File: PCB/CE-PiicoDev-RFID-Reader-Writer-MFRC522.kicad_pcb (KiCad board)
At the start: 2 copper layers, 25.4 x 52 mm, 19 parts, among them J1 , J2 , J3 Conn_PiicoDev_header_01x04_Ma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

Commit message: Update all
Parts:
- added C1: 22p NP0, Capacitor_SMD:C_0402_1005Metric, F.Cu at (152.4, 99.5)
- added C10: NP0 2%, Capacitor_SMD:C_0603_1608Metric, F.Cu at (153.1, 92.1)
- added C11: 100n, Capacitor_SMD:C_0402_1005Metric, F.Cu at (155.3, 99.5)
- added C12: 100n, Capacitor_SMD:C_0402_1005Metric, F.Cu at (158.2, 95.5)
- added C13: 100n, Capacitor_SMD:C_0402_1005Metric, F.Cu at (155.3, 97.5)
- added C2: 1n NP0 10%, Capacitor_SMD:C_0603_1608Metric, F.Cu at (143.9, 97.3)
- added C3: 100n X7R 10%, Capacitor_SMD:C_0402_1005Metric, F.Cu at (146.6, 106.0)
- added C4: 22p NP0, Capacitor_SMD:C_0402_1005Metric, F.Cu at (158.2, 97.5)
- added C5: 120p NP0 2%, Capacitor_SMD:C_0603_1608Metric, F.Cu at (149.1, 92.8)
- added C6: 120p NP0 2%, Capacitor_SMD:C_0603_1608Metric, F.Cu at (160.7, 108.3)
- added C7: C, Capacitor_SMD:C_0603_1608Metric, F.Cu at (140.9, 99.8)
- added C8: C, Capacitor_SMD:C_0603_1608Metric, F.Cu at (147.9, 97.3)
- added C9: NP0 2%, Capacitor_SMD:C_0603_1608Metric, F.Cu at (144.9, 99.8)
- added D2: LED, CoreElectronics_Components:LED_1206_3216Metric_ReverseMount_Hole1.8x2.4mm, F.Cu at (97.3, 96.6)
- added J4: Conn_01x01_Male, Connector_PinHeader_1.27mm:PinHeader_1x01_P1.27mm_Vertical, F.Cu at (150.7, 89.2)
- added J5: Conn_01x01_Male, CoreElectronics_Components:PiicoDev_header_1pin_INT_uninverted, F.Cu at (103.4, 120.9)
- added JP3: SolderJumper_2_Bridged, CoreElectronics_Components:SolderJumper-2_P1.3mm_Bridged_RoundedPad1.0x1.5mm, B.Cu at (86.2, 101.3)
- added L1: 1uH, Inductor_SMD:L_0402_1005Metric, F.Cu at (156.6, 93.5)
- added L2: 1uH, Inductor_SMD:L_0402_1005Metric, F.Cu at (152.4, 97.6)
- added NT1: Net-Tie_2, PiicoDev RFID MFRC522:NetTie-2_SMD_Pad0.25mm, F.Cu at (97.3, 86.4)
- added NT2: Net-Tie_2, PiicoDev RFID MFRC522:NetTie-2_SMD_Pad0.25mm, F.Cu at (97.3, 85.9)
- added NT3: Net-Tie_2, PiicoDev RFID MFRC522:NetTie-2_SMD_Pad0.25mm, F.Cu at (97.3, 85.4)
- added NT4: Net-Tie_2, PiicoDev RFID MFRC522:NetTie-2_SMD_Pad0.25mm, B.Cu at (97.3, 85.9)
- added NT5: Net-Tie_2, PiicoDev RFID MFRC522:NetTie-2_SMD_Pad0.25mm, B.Cu at (97.3, 86.4)
- added R4: 820R, Resistor_SMD:R_0603_1608Metric, F.Cu at (158.8, 88.8)
- added R5: R, Resistor_SMD:R_0603_1608Metric, F.Cu at (151.9, 95.3)
- added R6: R, Resistor_SMD:R_0603_1608Metric, F.Cu at (96.5, 88.1)
- added R7: R, Resistor_SMD:R_0603_1608Metric, F.Cu at (98.1, 88.1)
- added R8: R, Resistor_SMD:R_0402_1005Metric, F.Cu at (155.3, 95.5)
- added U1: MFRC522, Package_DFN_QFN:VQFN-32-1EP_5x5mm_P0.5mm_EP3.1x3.1mm, F.Cu at (97.3, 101.3)
- added Y1: 27.12MHz 12pF, Crystal:Crystal_SMD_3225-4Pin_3.2x2.5mm, F.Cu at (102.8, 95.6)
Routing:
- net /TURN6: track 0.00 -> 95.3 mm, vias 0 -> 1
- net /TURN1: track 0.00 -> 93.7 mm
- net /TURN2: track 0.00 -> 91.1 mm
- net /TURN5: track 0.00 -> 90.7 mm
- net /TURN3: track 0.00 -> 88.0 mm
- net /TURN4: track 0.00 -> 87.8 mm, vias 0 -> 1
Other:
- board text added: "Designed at Core Electronics by Peter Johnston"
- board text removed: "Designed at Core Electronics"

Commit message: Update
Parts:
- added C14: 100n, Capacitor_SMD:C_0402_1005Metric, F.Cu at (102.5, 103.1)
- added R9: 4k7, Resistor_SMD:R_0402_1005Metric, F.Cu at (102.1, 100.6)
- FID1, FID2: footprint Fiducial:Fiducial_1mm_Mask2mm -> CoreElectronics_Components:Fiducial_1mm_Mask2mm_No_Courtyard
- Y1: footprint Crystal:Crystal_SMD_3225-4Pin_3.2x2.5mm -> Crystal:Crystal_SMD_TXC_7M-4Pin_3.2x2.5mm
- moved R4 65.9 mm to (93.7, 98.9), turned to 90 degrees
- moved C4 64.5 mm to (93.9, 102.3), turned to 180 degrees
- moved L1 62.9 mm to (93.7, 91.7), turned to 90 degrees
- moved C6 62.4 mm to (101.3, 89.2)
- moved C13 59.4 mm to (95.9, 98.2), turned to 90 degrees
- moved C1 59.4 mm to (93.0, 101.0)
- moved R5 59.2 mm to (92.7, 95.9), turned to 90 degrees
- moved C12 57.3 mm to (101.0, 98.7), turned to 180 degrees
- moved C11 56.1 mm to (99.2, 97.8), turned to 90 degrees
- moved C5 55.9 mm to (93.3, 89.2), turned to 270 degrees
- moved C10 54.2 mm to (98.9, 91.5)
- moved R8 54.0 mm to (101.4, 95.1), turned to 180 degrees
- moved C3 52.3 mm to (94.9, 98.2), turned to 270 degrees
- moved L2 51.8 mm to (100.9, 91.7), turned to 90 degrees
- moved C2 51.8 mm to (92.1, 98.9), turned to 270 degrees
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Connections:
- C11 pad 1: Net-(C11-Pad1) -> +3V3
- C12 pad 1: Net-(C11-Pad1) -> +3V3
- C13 pad 1: Net-(C11-Pad1) -> +3V3
- Y1 pad 2: Net-(C1-Pad1) -> GND
- Y1 pad 3: (no net) -> Net-(C1-Pad1)
- Y1 pad 4: (no net) -> GND
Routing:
- net +3V3: track 45.1 -> 86.4 mm, vias 3 -> 7
- net /INT: track 0.00 -> 35.2 mm, vias 0 -> 3
- net GND: track 3.98 -> 26.1 mm, vias 3 -> 12
- net /RST: track 0.00 -> 11.1 mm, vias 0 -> 1
- net Net-(L2-Pad1): track 0.00 -> 9.61 mm, vias 0 -> 2
- net Net-(L1-Pad1): track 0.00 -> 9.19 mm
- net Net-(C5-Pad1): track 0.00 -> 8.56 mm
- net Net-(JP3-Pad2): track 0.00 -> 8.01 mm, vias 0 -> 1
- net /SCL: track 40.7 -> 47.9 mm, vias 2 -> 3
- net /SDA: track 42.0 -> 49.0 mm
- net Net-(C1-Pad1): track 0.00 -> 6.79 mm
- net Net-(C4-Pad1): track 0.00 -> 5.83 mm
- net Net-(C10-Pad2): track 0.00 -> 4.44 mm
- net Net-(C7-Pad1): track 0.00 -> 4.44 mm
- net Net-(C3-Pad2): track 0.00 -> 4.23 mm
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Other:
- board text added: "RFID Reader Writer MFRC522"
- board text removed: "Board Description Part Number"

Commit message: Update
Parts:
- added G4: Label_PCB_Art, PiicoDev RFID MFRC522:Label_Reset_Bar_Reverse Arrow, F.Cu at (105.3, 106.6)
- added G5: Label_PCB_Art, PiicoDev RFID MFRC522:Label_Reset_Bar, B.Cu at (105.3, 106.6)
- added NT10: Net-Tie_2, PiicoDev RFID MFRC522:NetTie-2_SMD_Pad0.25mm, B.Cu at (97.3, 86.6)
- added NT11: Net-Tie_2, PiicoDev RFID MFRC522:NetTie-2_SMD_Pad0.25mm, B.Cu at (97.3, 62.4)
- added NT6: Net-Tie_2_Top, PiicoDev RFID MFRC522:NetTie-2_SMD_Pad0.25mm, F.Cu at (97.3, 62.9)
- added NT7: Net-Tie_2_Top, PiicoDev RFID MFRC522:NetTie-2_SMD_Pad0.25mm, F.Cu at (97.3, 63.4)
- added NT8: Net-Tie_2_Top, PiicoDev RFID MFRC522:NetTie-2_SMD_Pad0.25mm, B.Cu at (97.3, 63.4)
- added NT9: Net-Tie_2_Top, PiicoDev RFID MFRC522:NetTie-2_SMD_Pad0.25mm, B.Cu at (97.3, 62.9)
- added Q1: BSS138, Package_TO_SOT_SMD:SOT-23, F.Cu at (92.5, 95.6)
- J4: footprint Connector_PinHeader_1.27mm:PinHeader_1x01_P1.27mm_Vertical -> Connector_PinHeader_2.54mm:PinHeader_1x01_P2.54mm_Vertical
- NT5: value Net-Tie_2 -> Net-Tie_2_Top; moved to F.Cu
- moved G2 26.6 mm to (97.3, 74.7)
- moved NT5 24.0 mm to (97.3, 62.4), turned to 0 degrees
- moved LOGO1 5.00 mm to (107.0, 101.2)
- moved R5 3.67 mm to (92.3, 92.3)
- moved R8 2.80 mm to (104.2, 95.0)
- moved G1 1.96 mm to (97.3, 66.5)
- moved NT1 0.70 mm to (97.3, 87.1)
- moved NT2 0.70 mm to (97.3, 86.6)
- moved NT3 0.70 mm to (97.3, 86.1)
- moved G3 0.39 mm to (97.3, 90.7)
- moved D2 0.30 mm to (97.3, 94.0)
- moved J4 0.30 mm to (108.3, 106.8)
- moved NT4 0.20 mm to (97.3, 86.1)
- moved C11 0.14 mm to (99.1, 97.7)
- moved C9 0.10 mm to (95.6, 91.5)
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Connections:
- net /RST renamed /~RST
- D2 pad 1: /INT -> Net-(4k7-Pad2)
- NT1 pad 1: /TURN1 -> /TURN1B
- NT1 pad 2: /TURN2 -> /TURN2A
- NT2 pad 1: /TURN2 -> /TURN2B
- NT2 pad 2: /TURN3 -> /TURN3A
- NT3 pad 1: /TURN3 -> /TURN3B
- NT3 pad 2: /TURN4 -> /TURN4A
- NT4 pad 1: /TURN4 -> /TURN4B
- NT4 pad 2: /TURN5 -> /TURN5A
- NT5 pad 1: /TURN5 -> /TURN1A
- NT5 pad 2: /TURN6 -> /TURN1B
- R6 pad 1: /TURN1 -> /TURN1A
- R7 pad 1: /TURN6 -> /TURN6B
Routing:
- net /TURN6: track 95.5 -> 0.00 mm, vias 1 -> 0
- net /TURN1: track 94.8 -> 0.00 mm
- net /TURN2: track 91.1 -> 0.00 mm
- net /TURN5: track 90.7 -> 0.00 mm
- net /TURN3: track 88.0 -> 0.00 mm
- net /TURN4: track 87.8 -> 0.00 mm, vias 1 -> 0
- net /TURN6A: track 0.00 -> 48.5 mm
- net /TURN1A: track 0.00 -> 48.3 mm
- net /TURN6B: track 0.00 -> 47.5 mm, vias 0 -> 1
- net /TURN1B: track 0.00 -> 47.2 mm
- net /TURN5A: track 0.00 -> 46.9 mm
- net /TURN2A: track 0.00 -> 46.5 mm
- net /TURN5B: track 0.00 -> 45.9 mm
- net /TURN2B: track 0.00 -> 45.7 mm
- net /TURN4A: track 0.00 -> 45.6 mm, vias 0 -> 1
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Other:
- board text added: "INT LED"
- board text added: "piico.dev/p16"
- board text removed: "piico.dev/pXX"

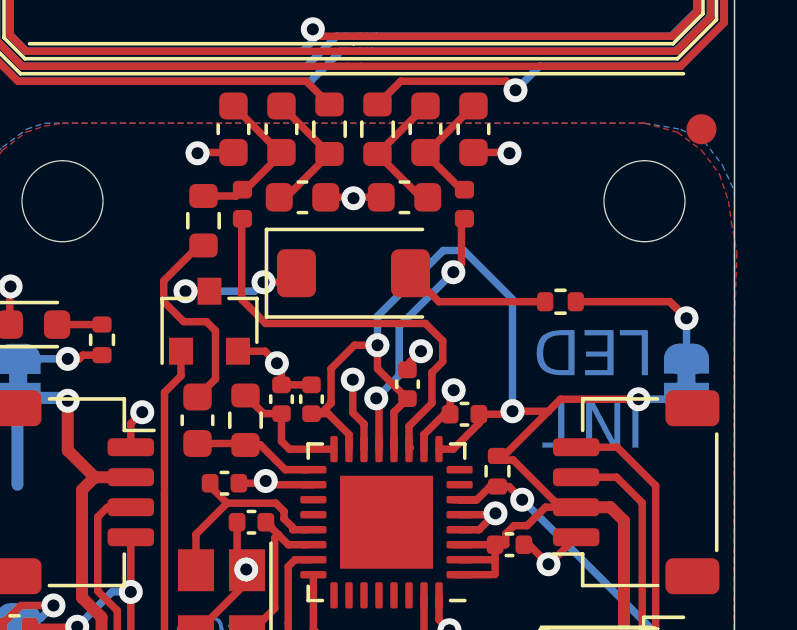
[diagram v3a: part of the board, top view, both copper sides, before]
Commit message: Add R10
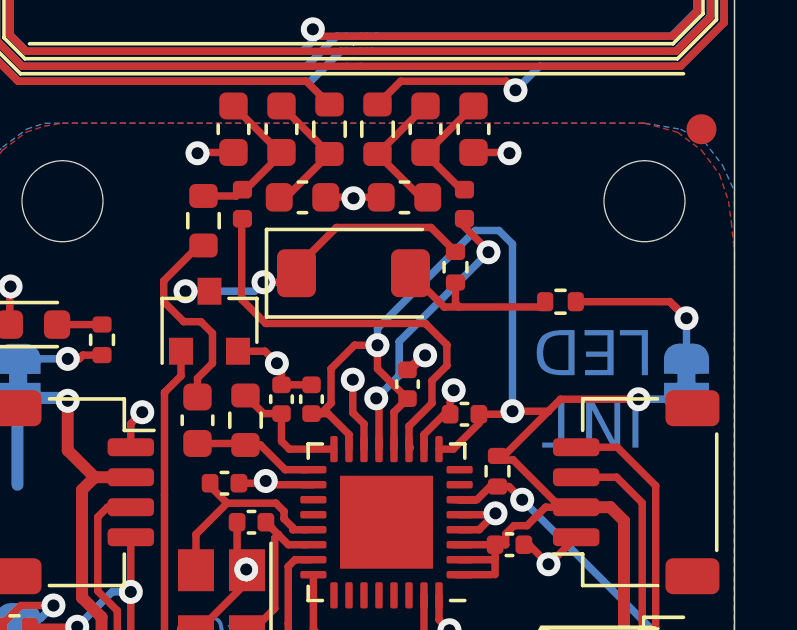
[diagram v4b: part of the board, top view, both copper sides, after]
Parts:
- added R10: 4k7, Resistor_SMD:R_0402_1005Metric, F.Cu at (100.7, 93.8)
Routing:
- net Net-(D2-Pad1): track 4.62 -> 11.0 mm
- net +3V3: track 90.1 -> 91.5 mm
- net Net-(D2-Pad2): track 5.84 -> 6.85 mm
- net Net-(L2-Pad1): track 9.01 -> 9.59 mm

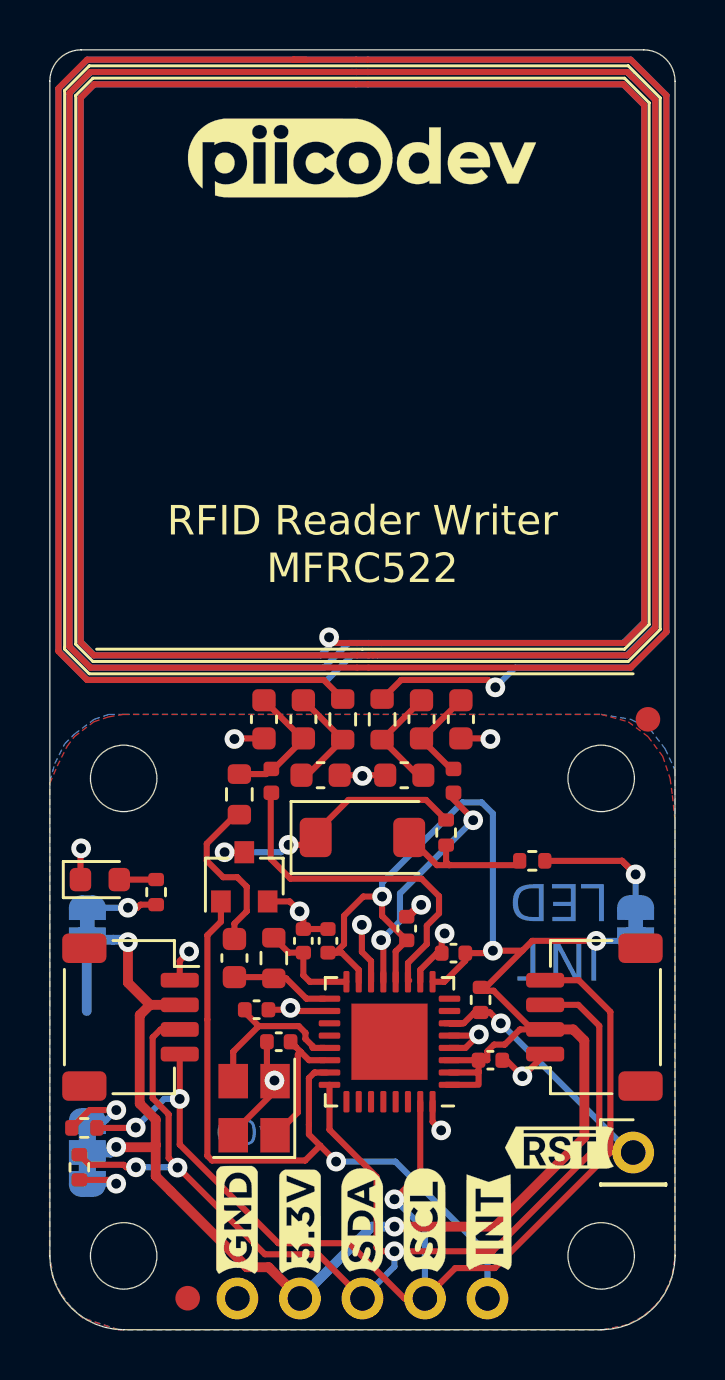
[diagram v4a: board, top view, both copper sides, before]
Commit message: Change v00 to v01
Halve the coil length.
Make wider coil tracks.
Add test points.
Add I2C series resistor.
Change inductors from 0402 to 0603.
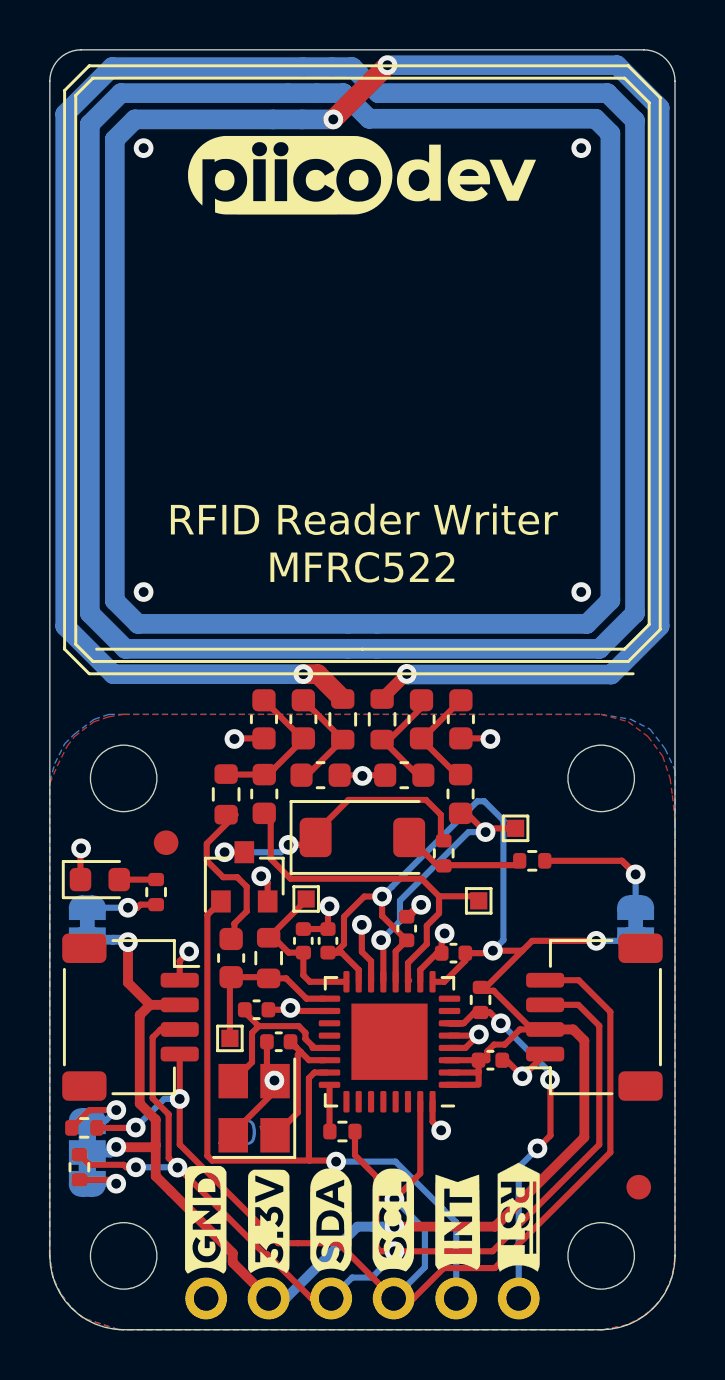
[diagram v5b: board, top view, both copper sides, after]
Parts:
- removed NT1, NT2, NT3: Net-Tie_2, PiicoDev RFID MFRC522:NetTie-2_SMD_Pad0.25mm
- removed NT5, NT6, NT7: Net-Tie_2_Top, PiicoDev RFID MFRC522:NetTie-2_SMD_Pad0.25mm
- added R11: 120R, Resistor_SMD:R_0402_1005Metric, F.Cu at (96.5, 106.0)
- added TP1: TestPoint, CoreElectronics_Components:TestPoint_Pad_0.7x0.7mm, F.Cu at (91.9, 102.2)
- added TP2: TestPoint, CoreElectronics_Components:TestPoint_Pad_0.7x0.7mm, F.Cu at (95.0, 96.5)
- added TP3: TestPoint, CoreElectronics_Components:TestPoint_Pad_0.7x0.7mm, F.Cu at (102.0, 96.6)
- added TP4: TestPoint, CoreElectronics_Components:TestPoint_Pad_0.7x0.7mm, F.Cu at (103.5, 93.7)
- J4: footprint Connector_PinHeader_2.54mm:PinHeader_1x01_P2.54mm_Vertical -> CoreElectronics_Components:PiicoDev_header_1pin
- L1, L2: footprint Inductor_SMD:L_0402_1005Metric -> Inductor_SMD:L_0603_1608Metric
- NT10, NT11, NT4, NT8, NT9: footprint PiicoDev RFID MFRC522:NetTie-2_SMD_Pad0.25mm -> PiicoDev RFID MFRC522:NetTie-2_SMD_Pad0.80mm
- R8: value R -> 4k7
- moved FID2 20.2 mm to (89.3, 94.3)
- moved FID1 18.9 mm to (108.5, 108.3)
- moved J4 7.54 mm to (103.6, 112.8)
- moved NT11 3.89 mm to (94.2, 64.9)
- moved G4 3.27 mm to (103.6, 109.5), turned to 270 degrees
- moved G5 3.17 mm to (103.6, 109.3), turned to 90 degrees
- moved NT9 2.59 mm to (94.8, 63.8)
- moved NT8 1.95 mm to (95.5, 62.7)
- moved NT10 1.28 mm to (97.3, 85.4)
- moved J3 1.27 mm to (90.9, 112.8)
- moved J5 1.27 mm to (101.1, 112.8)
- moved R10 0.85 mm to (100.6, 94.7)
- moved G1 0.70 mm to (97.3, 67.2)
- moved L1 0.61 mm to (93.3, 92.3)
- moved L2 0.61 mm to (101.3, 92.3)
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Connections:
- NT8 pad 1: /TURN4A -> /TURN1A
- U1 pad 24: /SDA -> Net-(R11-Pad1)
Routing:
- net /TURN1B: track 47.2 -> 0.00 mm
- net /TURN2A: track 46.5 -> 0.00 mm
- net /TURN2B: track 45.7 -> 0.00 mm
- net /TURN4A: track 45.6 -> 0.00 mm, vias 1 -> 0
- net /TURN3A: track 45.0 -> 0.00 mm
- net /TURN3B: track 44.1 -> 0.00 mm
- net /TURN6A: track 48.5 -> 35.4 mm
- net /TURN5A: track 46.9 -> 39.5 mm
- net /~RST: track 11.1 -> 16.2 mm, vias 1 -> 3
- net /TURN1A: track 48.3 -> 43.7 mm, vias 0 -> 1
- net /TURN5B: track 45.9 -> 41.4 mm
- net /SDA: track 49.0 -> 46.4 mm
- net Net-(C2-Pad2): track 4.02 -> 6.59 mm
- net +3V3: track 91.5 -> 88.9 mm
- net /TURN6B: track 47.5 -> 49.7 mm, vias 1 -> 3
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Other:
- net class Antenna added: clearance 0.2, trace_width 0.8, via_dia 0.8, via_drill 0.4
- board text added: "v01"
- board text removed: "v00"

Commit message: Update
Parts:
- removed R7: R, Resistor_SMD:R_0603_1608Metric
- added C15: 270p NP0 2%, Capacitor_SMD:C_0603_1608Metric, F.Cu at (96.5, 89.2)
- added C16: 270p NP0 2%, Capacitor_SMD:C_0603_1608Metric, F.Cu at (98.1, 89.2)
- added JP4: SolderJumper_2_Open, CoreElectronics_Components:SolderJumper-2_P1.3mm_Open_RoundedPad1.0x1.5mm, B.Cu at (108.4, 106.2)
- C10, C9: value NP0 2% -> 270p NP0 2%
- C5, C6: value 120p NP0 2% -> 62p NP0 2%
- C7, C8: value C -> 56p
- R1, R2, R3, R9: value 4k7 -> 10k
- R5: value R -> 470R
- R6: value R -> 10k; footprint Resistor_SMD:R_0603_1608Metric -> Resistor_SMD:R_0402_1005Metric
- TP1, TP2, TP3, TP4: moved to B.Cu
- moved R6 18.1 mm to (102.5, 106.4)
- moved G2 6.28 mm to (97.3, 81.0)
- moved C5 3.39 mm to (95.7, 91.6), turned to 0 degrees
- moved C6 3.39 mm to (98.9, 91.6), turned to 180 degrees
- moved C10 2.38 mm to (99.7, 89.2), turned to 90 degrees
- moved C9 2.38 mm to (94.9, 89.2), turned to 270 degrees
- moved TP1 2.16 mm to (89.8, 102.9)
- moved TP4 1.90 mm to (102.0, 94.9)
- moved C7 1.60 mm to (93.3, 89.2)
- moved C8 1.60 mm to (101.3, 89.2)
- moved TP2 1.43 mm to (93.6, 96.7)
- moved TP3 1.02 mm to (102.0, 97.6)
- moved R11 0.88 mm to (96.5, 106.9)
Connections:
- C10 pad 2: Net-(C10-Pad2) -> /TURN6B
- C7 pad 1: Net-(C7-Pad1) -> /TURN1A
- C8 pad 1: Net-(C10-Pad2) -> /TURN6B
- C9 pad 1: Net-(C7-Pad1) -> /TURN1A
- R6 pad 1: /TURN1A -> Net-(JP4-Pad2)
- R6 pad 2: Net-(C7-Pad1) -> GND
- U1 pad 25: Net-(U1-Pad25) -> GND
- U1 pad 26: Net-(U1-Pad26) -> GND
- U1 pad 27: Net-(U1-Pad27) -> GND
- U1 pad 28: Net-(U1-Pad28) -> +3V3
- U1 pad 29: Net-(U1-Pad29) -> GND
- U1 pad 30: Net-(U1-Pad30) -> Net-(JP4-Pad2)
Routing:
- net Net-(JP4-Pad2): track 0.00 -> 12.4 mm, vias 0 -> 3
- net +3V3: track 88.9 -> 97.5 mm, vias 6 -> 9
- net GND: track 30.6 -> 38.5 mm, vias 15 -> 17
- net Net-(C10-Pad2): track 4.61 -> 0.00 mm
- net Net-(C7-Pad1): track 4.44 -> 0.00 mm
- net /TURN1A: track 43.7 -> 46.9 mm
- net /TURN6B: track 49.7 -> 52.9 mm
- net Net-(C2-Pad2): track 6.59 -> 8.92 mm, vias 0 -> 1
- net Net-(L1-Pad1): track 15.2 -> 16.2 mm, vias 0 -> 1
- net Net-(C5-Pad1): track 5.95 -> 5.01 mm
- net Net-(R11-Pad1): track 1.90 -> 2.80 mm
- net Net-(C3-Pad2): track 6.44 -> 7.30 mm, vias 0 -> 1
- net Net-(C6-Pad1): track 3.98 -> 3.16 mm
- net /SDA: track 46.4 -> 45.7 mm
- net /SCL: track 48.4 -> 49.1 mm
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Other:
- board text added: "v02"
- board text removed: "v01"

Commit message: Improve Artwork
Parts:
- removed G2: LOGO_CoreElectronics_no-text, CoreElectronics_Artwork:CoreElectronics_logo_5mm
- added G6: Label_PCB_Art, PiicoDev RFID MFRC522:Art_1, B.Cu at (97.3, 74.8)
- added G7: Label_PCB_Art, PiicoDev RFID MFRC522:Art_2, F.Cu at (97.3, 74.2)
